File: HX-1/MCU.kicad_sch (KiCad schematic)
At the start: 31 parts, among them J10 Conn_01x24, J12 USART, J3 I2C, J4 SPI, J8 UART, J9 Conn_01x24, SW1 BOOT0, U1 STM32H723ZGT6

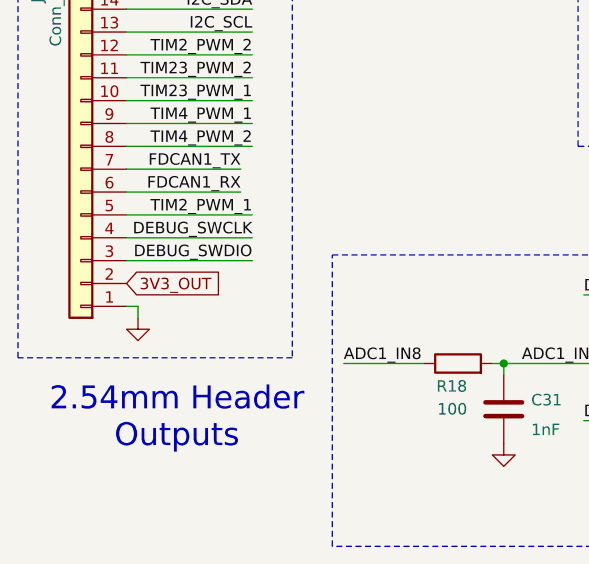
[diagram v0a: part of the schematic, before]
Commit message: remove 3V3 out and replace with standard 3V3 in.
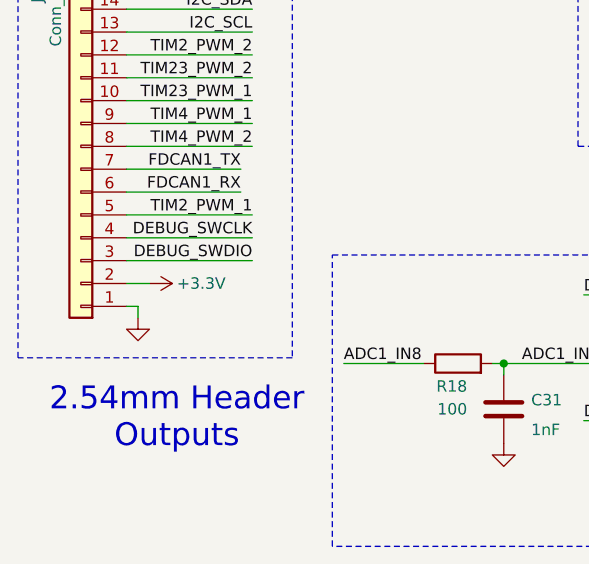
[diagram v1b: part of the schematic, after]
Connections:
- net 3V3_OUT is gone; now on net +3.3V: J9.2 (Pin_2)

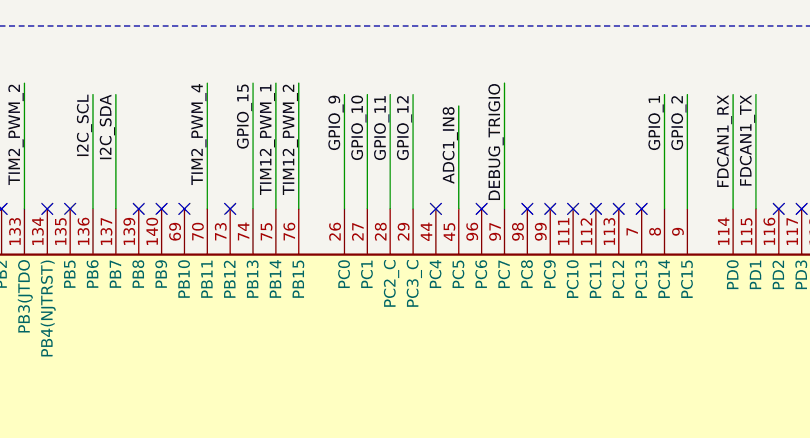
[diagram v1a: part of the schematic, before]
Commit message: remove GPIO 12 from MCU and firmware
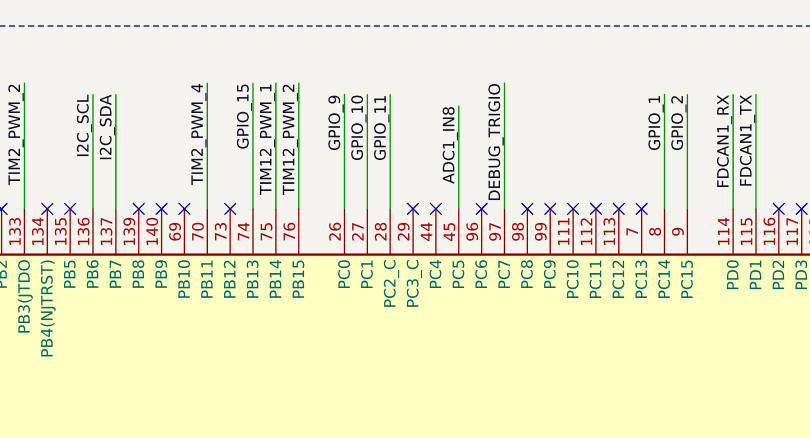
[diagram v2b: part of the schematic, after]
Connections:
- net GPIO_12: no longer names the net of U1.29 (PC3_C)
- no-connect marks 48 -> 49

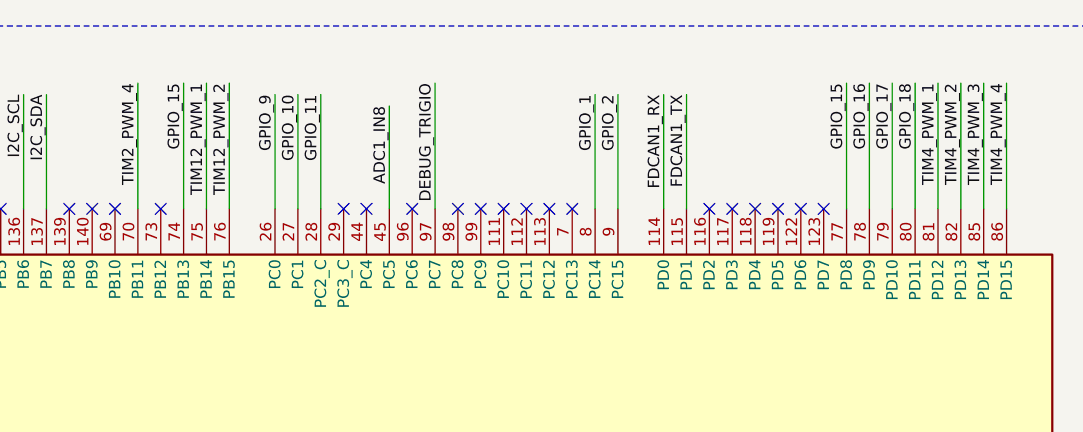
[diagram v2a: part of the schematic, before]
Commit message: remove forgotten excess GPIO pins
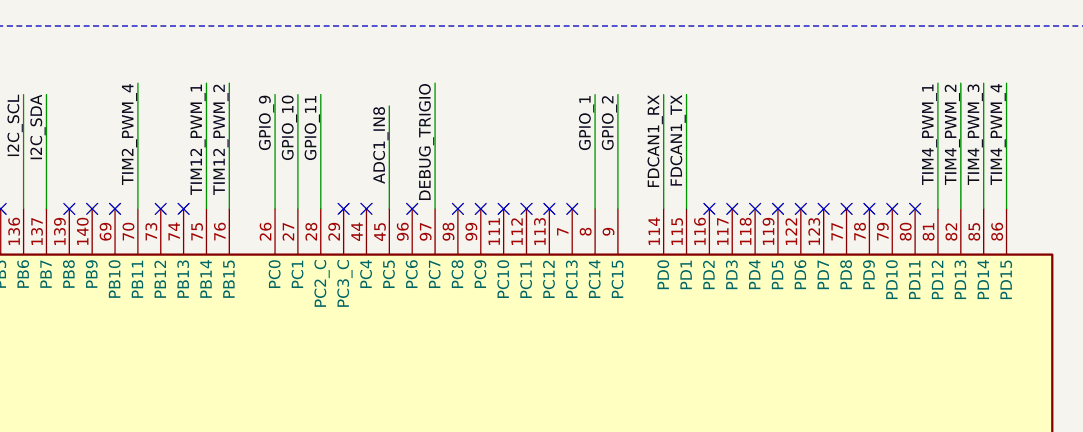
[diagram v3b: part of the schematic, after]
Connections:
- net GPIO_15: no longer names the net of U1.74 (PB13)
- net GPIO_15: no longer U1.77 (PD8)
- net GPIO_16: no longer names the net of U1.78 (PD9)
- net GPIO_17: no longer names the net of U1.79 (PD10)
- net GPIO_18: no longer names the net of U1.80 (PD11)
- no-connect marks 49 -> 54

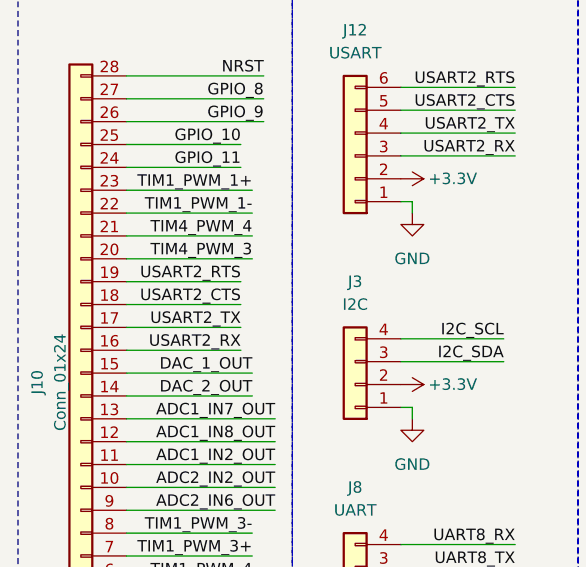
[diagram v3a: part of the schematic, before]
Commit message: route USART traces, flip pin 18 and pin 19 on left header
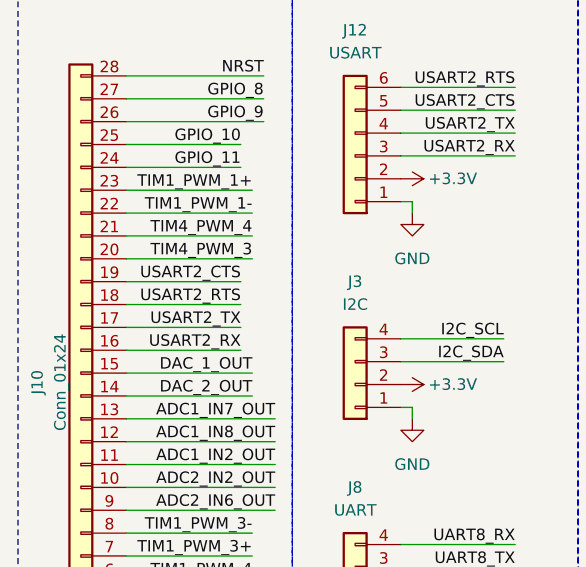
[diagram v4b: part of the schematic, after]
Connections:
- net USART2_CTS: now also J10.19 (Pin_19); no longer J10.18 (Pin_18)
- net USART2_RTS: now also J10.18 (Pin_18); no longer J10.19 (Pin_19)

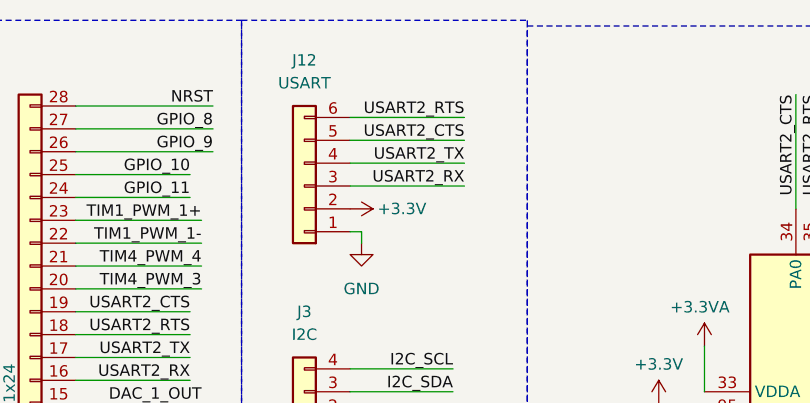
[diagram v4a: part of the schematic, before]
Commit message: complete route of left side of board, flip cts and rts pins on jst connector
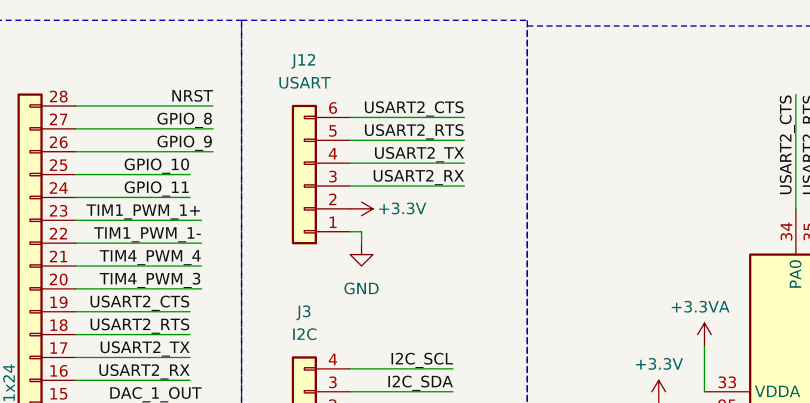
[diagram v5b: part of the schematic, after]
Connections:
- net USART2_CTS: now also J12.6 (Pin_6); no longer J12.5 (Pin_5)
- net USART2_RTS: now also J12.5 (Pin_5); no longer J12.6 (Pin_6)

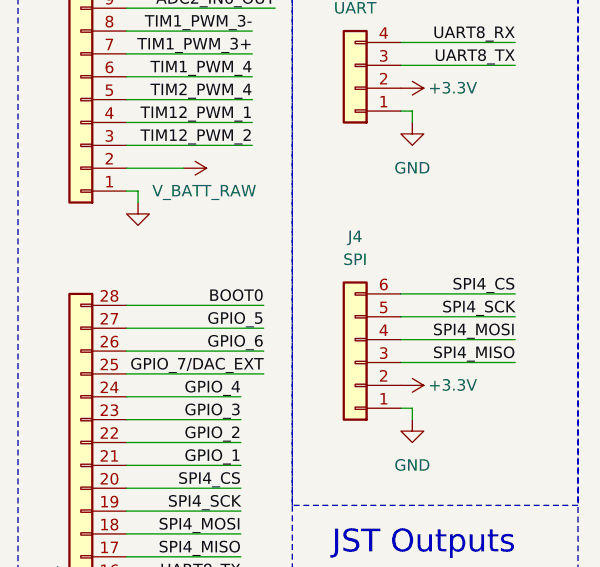
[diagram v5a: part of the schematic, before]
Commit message: replace right header pin for BOOT with GND, remove PIN control of BOOT for simplicity
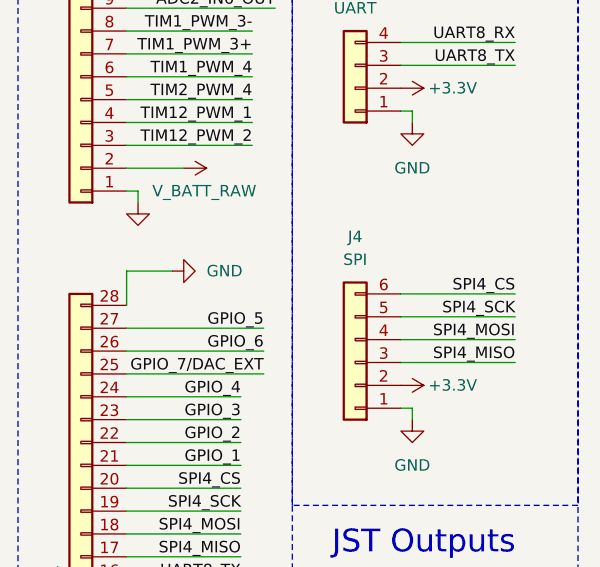
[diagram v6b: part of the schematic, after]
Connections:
- net BOOT0: no longer J9.28 (Pin_28)
- net GND: now also J9.28 (Pin_28)

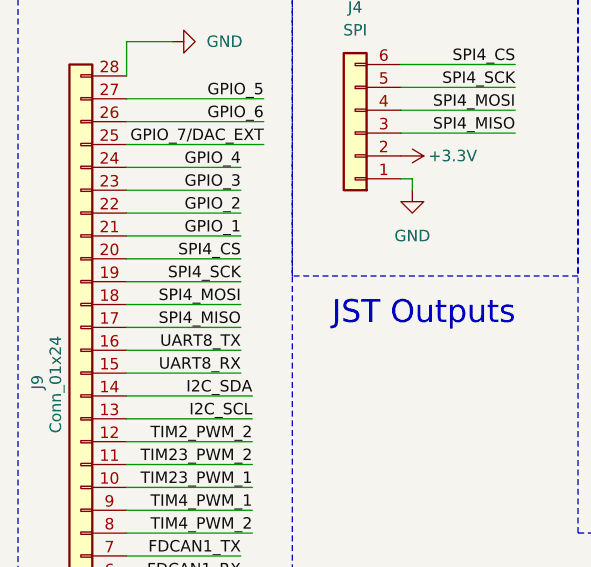
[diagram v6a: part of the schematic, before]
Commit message: change pin ordering of SPI on left header for better routing, route some of the left traces
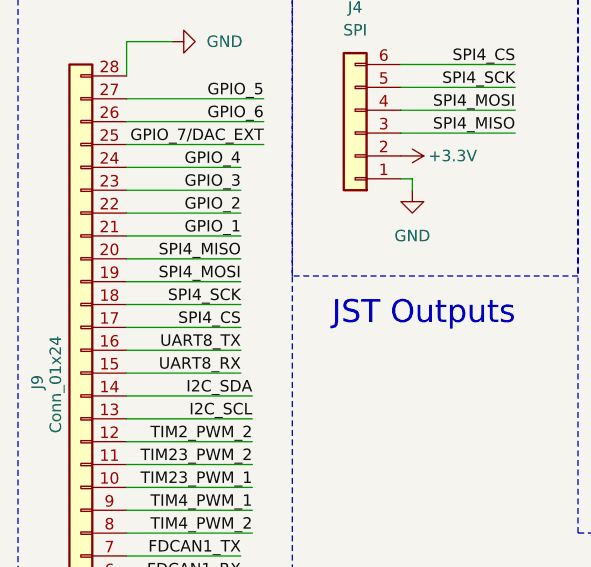
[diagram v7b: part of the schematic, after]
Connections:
- net SPI4_CS: now also J9.17 (Pin_17); no longer J9.20 (Pin_20)
- net SPI4_MISO: now also J9.20 (Pin_20); no longer J9.17 (Pin_17)
- net SPI4_MOSI: now also J9.19 (Pin_19); no longer J9.18 (Pin_18)
- net SPI4_SCK: now also J9.18 (Pin_18); no longer J9.19 (Pin_19)

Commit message: flip TWM_PWM+1 and -1 for better routing, improve routing for better gnd planes
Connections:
- net TIM1_PWM_1+: now also J10.22 (Pin_22); no longer J10.23 (Pin_23)
- net TIM1_PWM_1-: now also J10.23 (Pin_23); no longer J10.22 (Pin_22)
